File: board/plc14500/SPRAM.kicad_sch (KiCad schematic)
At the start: 26 parts, among them U12 4011, U13 4099, U14 4051

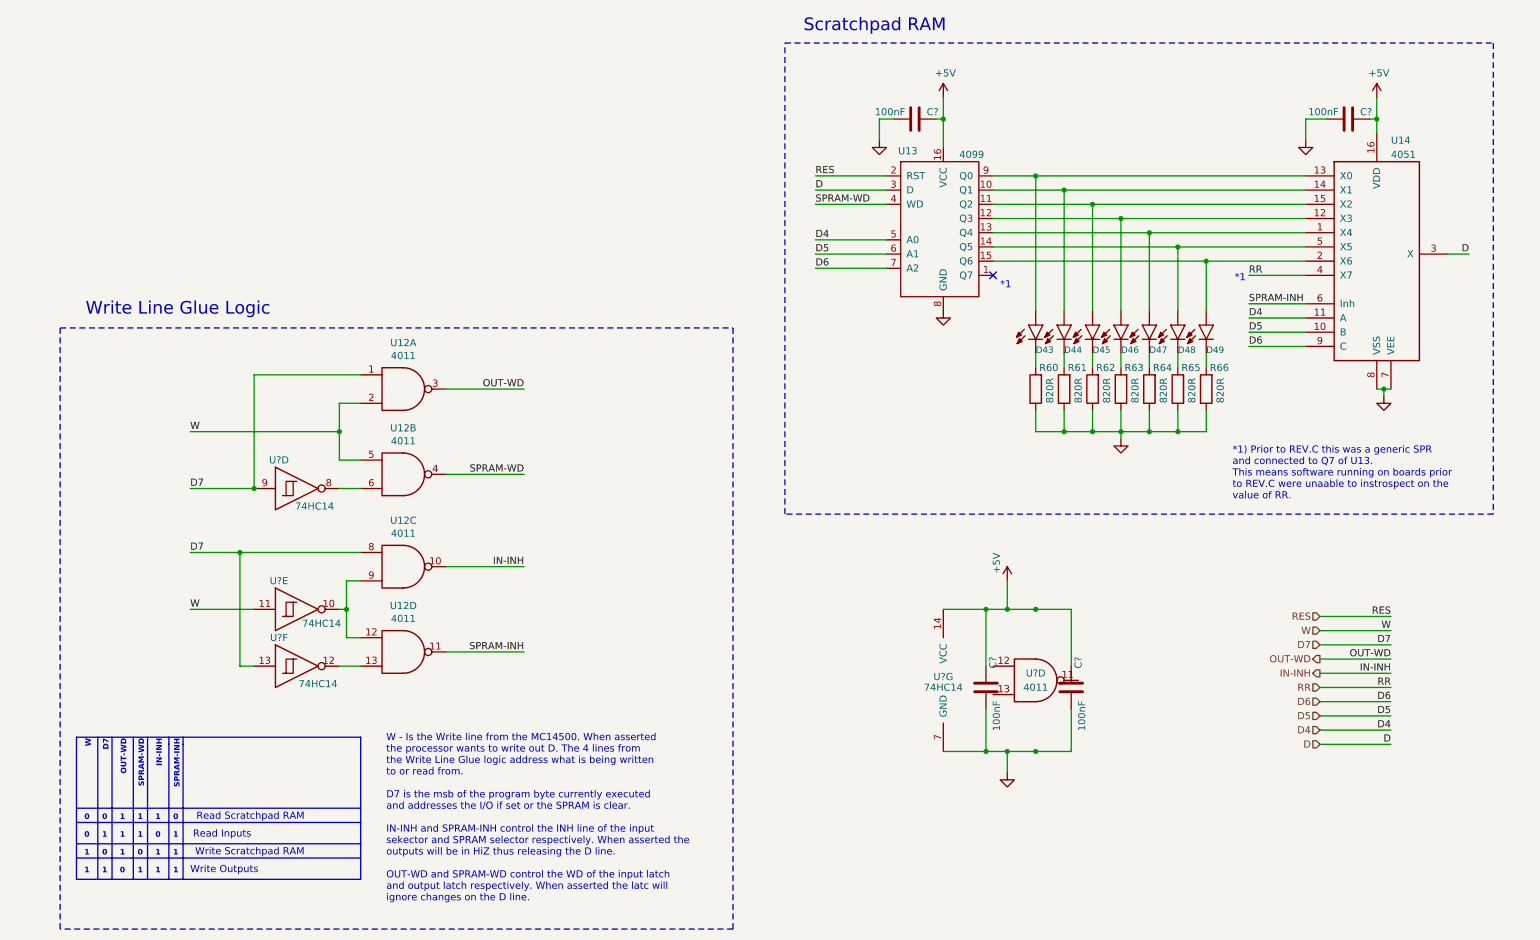
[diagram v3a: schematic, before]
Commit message: Fix issues on REV.D0
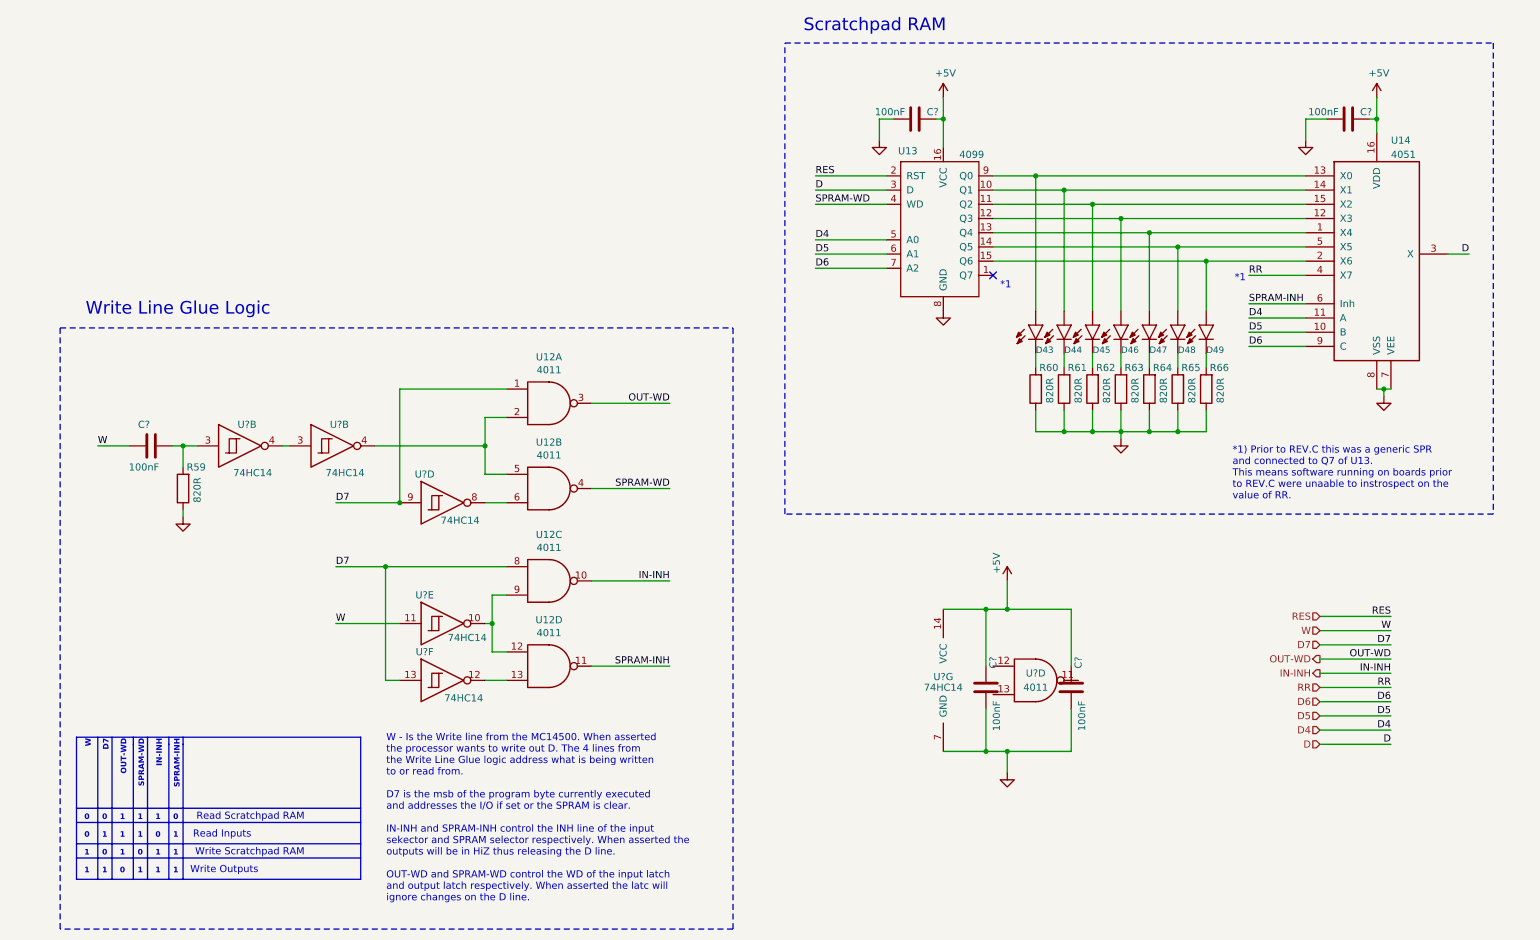
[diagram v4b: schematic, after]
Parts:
- added C?: 100nF, Capacitor_THT:C_Rect_L7.2mm_W2.5mm_P5.00mm_FKS2_FKP2_MKS2_MKP2, symbol Device:C
- added R59: 820R, Resistor_THT:R_Axial_DIN0204_L3.6mm_D1.6mm_P7.62mm_Horizontal, symbol Device:R
- added U? (x2): 74HC14, Package_DIP:DIP-14_W7.62mm_LongPads, symbol plc14500:74HC14
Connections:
- net GND: now also R59.1
- net W: now also C?.2; no longer U12.2, U12.5
- new net: U12.2, U12.5, U?.4
- new net: U?.3, U?.4
- new net: C?.1, R59.2, U?.3
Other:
- moved on the sheet: U12A, U12B, U12C, U12D, U?D, U?E, U?F
